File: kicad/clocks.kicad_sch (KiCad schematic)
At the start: 0 parts

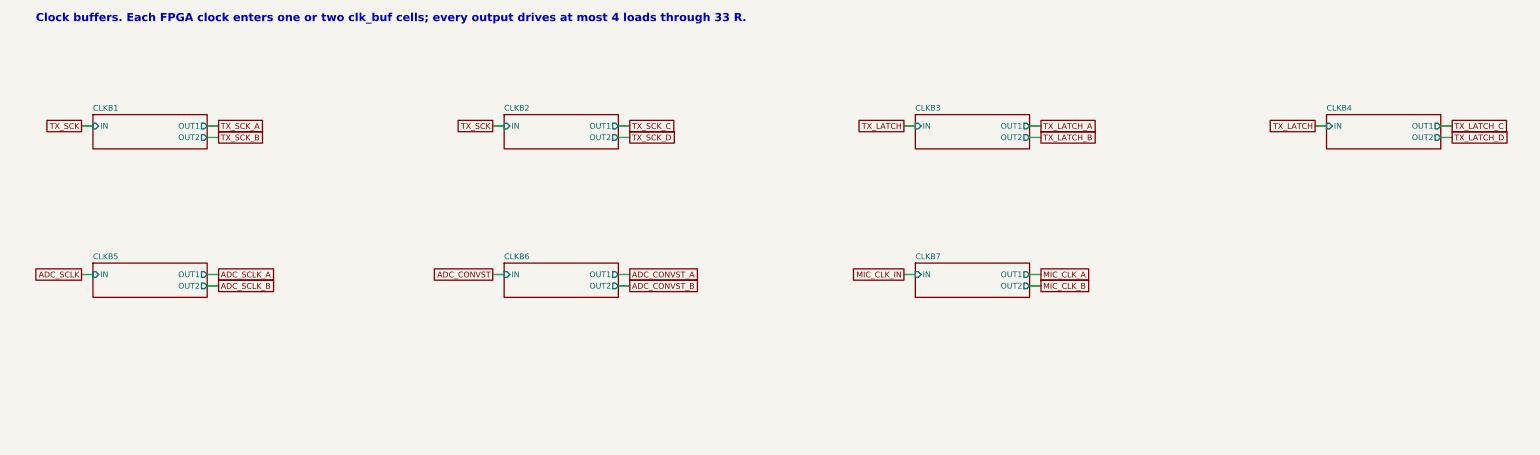
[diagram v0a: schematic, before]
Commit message: Switch to 16 x TLV320ADC5140, +3V3A rail, 3 A buck, datasheet library, transducer DNP
- ADC: 8 x AD7606C-16 ($470/board) -> 16 x TI TLV320ADC5140 at 192 kSPS ($50/board): TDM slave on a
  shared BCLK/FSYNC, I2C (SCL + 4 SDA groups), 2k/1k + 100 nF input network; project symbol from
  scripts/make_symbols.py; 9 clock buffers; J2 remapped
- power: +3V3A (second TPS7A4700, ANY-OUT 3.3 V); +5V buck TPS54202 -> TPS54302 (3 A), L1 10 uH 5 A
- checks and simulations updated for the new ADC input (all 18 checks and 10 sims pass)
- docs/datasheets: a PDF for every part, kept in step by scripts/datasheets.py (run by bom.py)
- design brief section 5a: interface bandwidth budget (no bus is a bottleneck; TX_EDGE = 1)
- CUSA-TR65 marked DNP for JLCPCB (hand-soldered), priced at DigiKey 100+
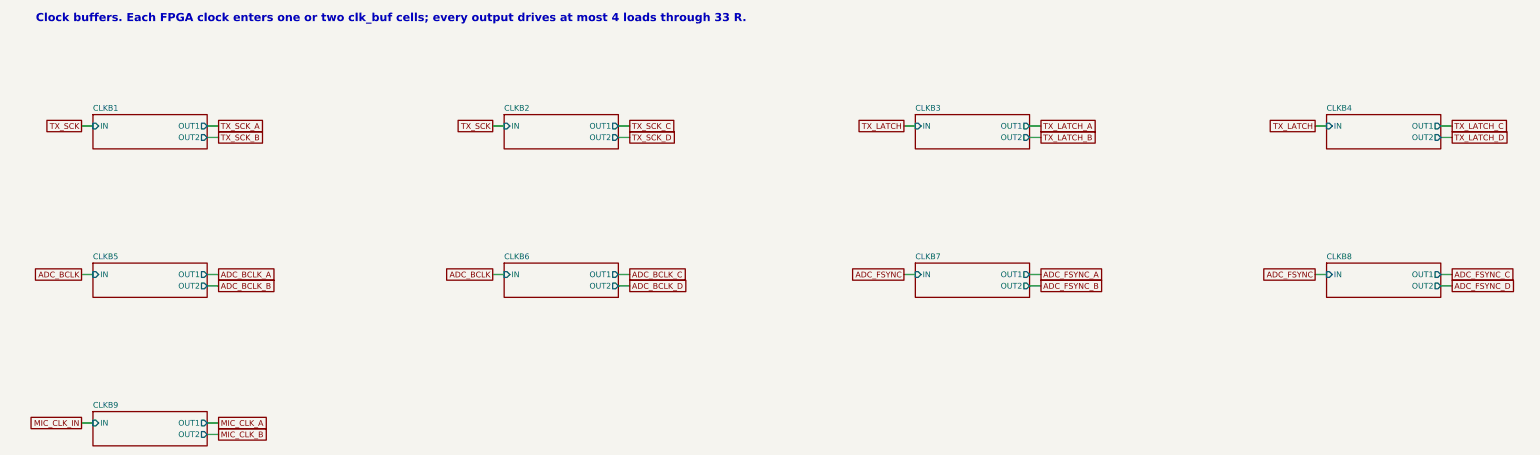
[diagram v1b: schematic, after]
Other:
- added sheet CLKB8 (clk_buf.kicad_sch)
- added sheet CLKB9 (clk_buf.kicad_sch)
- title: Clock buffers: 7 x 74LVC2G34 at the FPGA headers -> Clock buffers: 9 x 74LVC2G34 at the FPGA headers

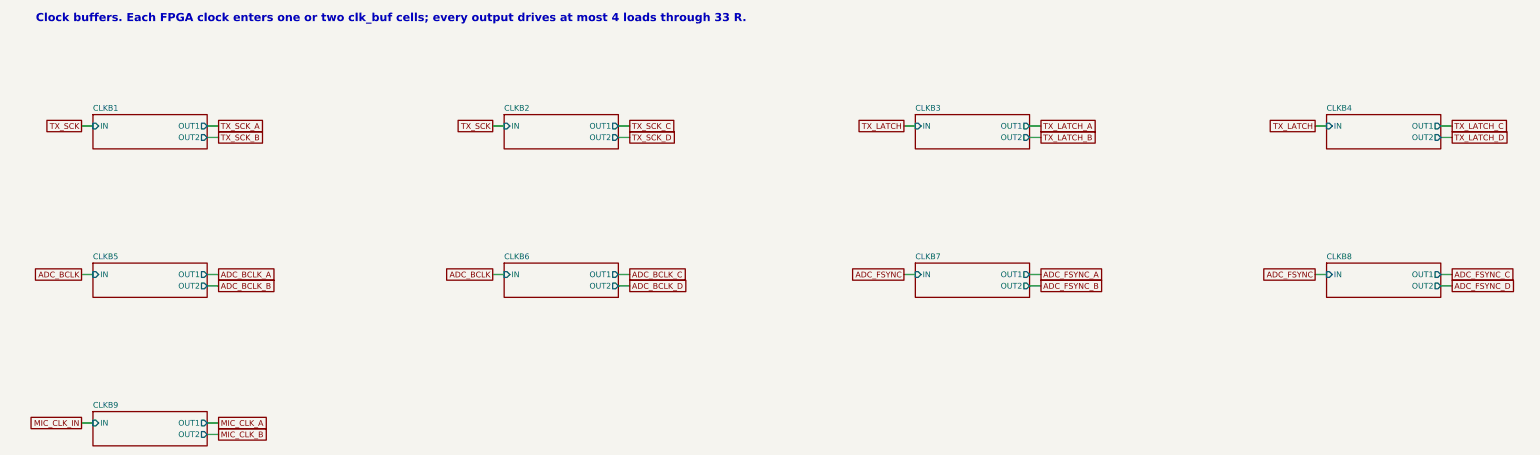
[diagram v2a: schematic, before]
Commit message: Block-first routing: all repeated blocks routed and passing, power input and +-6V5 hand-routed
Schematic
- TX groups and ADC inputs numbered in order (TXG01 = DRV1-4, ADC IN1..4 = RX1..4).
- Power sheets renumbered 1-8 with real references; eFuse RTN no longer tied to GND (TPS2660 9.3.5.5).
- Damped 100 uF bulk caps at the far ends of VIN (C50) and +5V (C51); header clock RC filters removed;
  switch-node snubbers kept as DNP footprints.

Layout and routing
- New routing toolchain: route.py (block stages), block_routes.py (hand-made block routes), maze.py
  (45-degree grid router with rip-up and a per-net time budget), route_lib.py (bend45, chamfer, copper
  checks), block_check.py (DRC and internal nets per block instance), board/cell views.
- Channel, ADC, TX group, clock buffer, enable buffer, mic and header blocks routed and passing
  block_check; no right-angle corners left.
- Designed TX control bus; SDI taps keep 0.7 mm from clock copper.
- Power: 12 V input (eFuse, RTN island, FLT via the front copper) and TPS65131 +-6V5 section with fixed
  templates and hand routing; each power section counts as its own block; the +3V3 LED overflows into
  the gap beside its section.

docs/routing_and_emi.md describes the routing and EMI rules; sim/mic_clock_si adds the mic clock check.
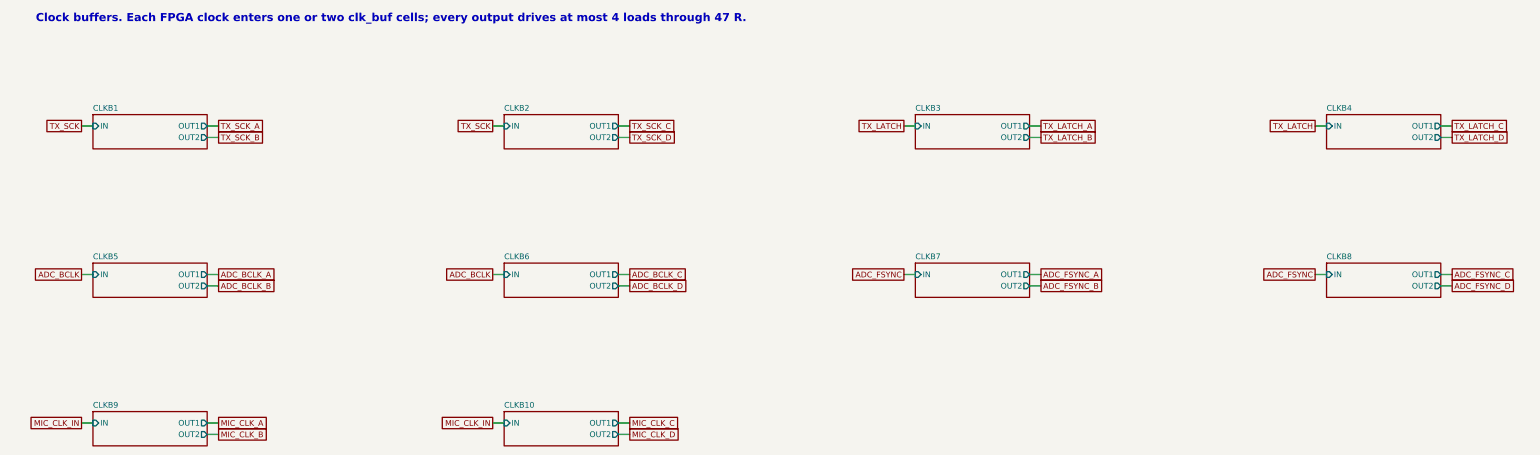
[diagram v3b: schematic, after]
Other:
- added sheet CLKB10 (clk_buf.kicad_sch)
- note added: "Clock buffers. Each FPGA clock enters one or two clk_buf cells; every output drives at most 4 loads through 47 R."
- note removed: "Clock buffers. Each FPGA clock enters one or two clk_buf cells; every output drives at most 4 loads through 33 R."
- title: Clock buffers: 9 x 74LVC2G34 at the FPGA headers -> Clock buffers: 10 x 74LVC2G34
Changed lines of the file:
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@@
 	(paper "A3")
 	(title_block
-		(title "Clock buffers: 9 x 74LVC2G34 at the FPGA headers")
+		(title "Clock buffers: 10 x 74LVC2G34")
 		(date "2026-10-24")
 		(rev "1")
 		(company "Hybrid 8x8 ultrasonic AESA")
 	)
-	(text "Clock buffers. Each FPGA clock enters one or two clk_buf cells; every output drives at most 4 loads through 33 R."
+	(text "Clock buffers. Each FPGA clock enters one or two clk_buf cells; every output drives at most 4 loads through 47 R."
 		(exclude_from_sim no)
 		(at 38.10 30.48 0)
@@
 				)
 			)
+		)
+	)
+	(wire
+		(pts
+			(xy 142.24 119.38) (xy 139.70 119.38)
+		)
+		(stroke
+			(width 0)
+			(type default)
+		)
+	)
+	(global_label "MIC_CLK_IN"
+		(shape passive)
+		(at 139.70 119.38 180)
+		(effects
+			(font
+				(size 1.27 1.27)
+			)
+			(justify right)
+		)
+	)
+	(wire
+		(pts
+			(xy 167.64 119.38) (xy 170.18 119.38)
+		)
+		(stroke
+			(width 0)
+			(type default)
+		)
+	)
+	(global_label "MIC_CLK_C"
+		(shape passive)
+		(at 170.18 119.38 0)
+		(effects
+			(font
+				(size 1.27 1.27)
+			)
+			(justify left)
+		)
+	)
+	(wire
+		(pts
+			(xy 167.64 121.92) (xy 170.18 121.92)
+		)
+		(stroke
+			(width 0)
+			(type default)
+		)
+	)
+	(global_label "MIC_CLK_D"
+		(shape passive)
+		(at 170.18 121.92 0)
+		(effects
+			(font
+				(size 1.27 1.27)
+			)
+			(justify left)
+		)
+	)
+	(sheet
+		(at 142.24 116.84)
+		(size 25.40 7.62)
+		(fields_autoplaced yes)
+		(stroke
+			(width 0.1524)
+			(type solid)
+		)
+		(fill
+			(color 0 0 0 0.0000)
+		)
+		(property "Sheetname" "CLKB10"
+			(at 142.24 116.13 0)
+			(effects
+				(font
+					(size 1.27 1.27)
+					(bold no)
+				)
+				(justify left bottom)
+			)
+		)
+		(property "Sheetfile" "clk_buf.kicad_sch"
+			(at 142.24 125.05 0)
+			(effects
+				(font
+					(size 1.27 1.27)
+				)
+				(justify left top)
+				(hide yes)
+			)
+		)
+		(pin "IN" input
+			(at 142.24 119.38 180)
+			(effects
+				(font
+					(size 1.27 1.27)
+				)
+				(justify left)
+			)
+		)
+		(pin "OUT1" output
+			(at 167.64 119.38 0)
+			(effects
+				(font
+					(size 1.27 1.27)
+				)
+				(justify right)
+			)
+		)
+		(pin "OUT2" output
+			(at 167.64 121.92 0)
+			(effects
+				(font
+					(size 1.27 1.27)
+				)
+				(justify right)
+			)
+		)
+		(instances
+			(project "aesa"
+				(path "/35d88121-1d5f-4a62-9009-788ea6bf93dd/a66a9929-b3db-5b77-9fc6-8a8088c45b7b"
+					(page "13")
+				)
+			)
